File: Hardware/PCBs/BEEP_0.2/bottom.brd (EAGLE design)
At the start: 85.7 x 100 mm, 60 parts, among them IC1 74HCT00D, Q1 DMN2075U, Q2 IRLML2244, Q5 IRLML2244, Q6 IRLML2244, Q8 IRLML2244, U1 LM239AMDREP, U2 ATTINY10-TSHR

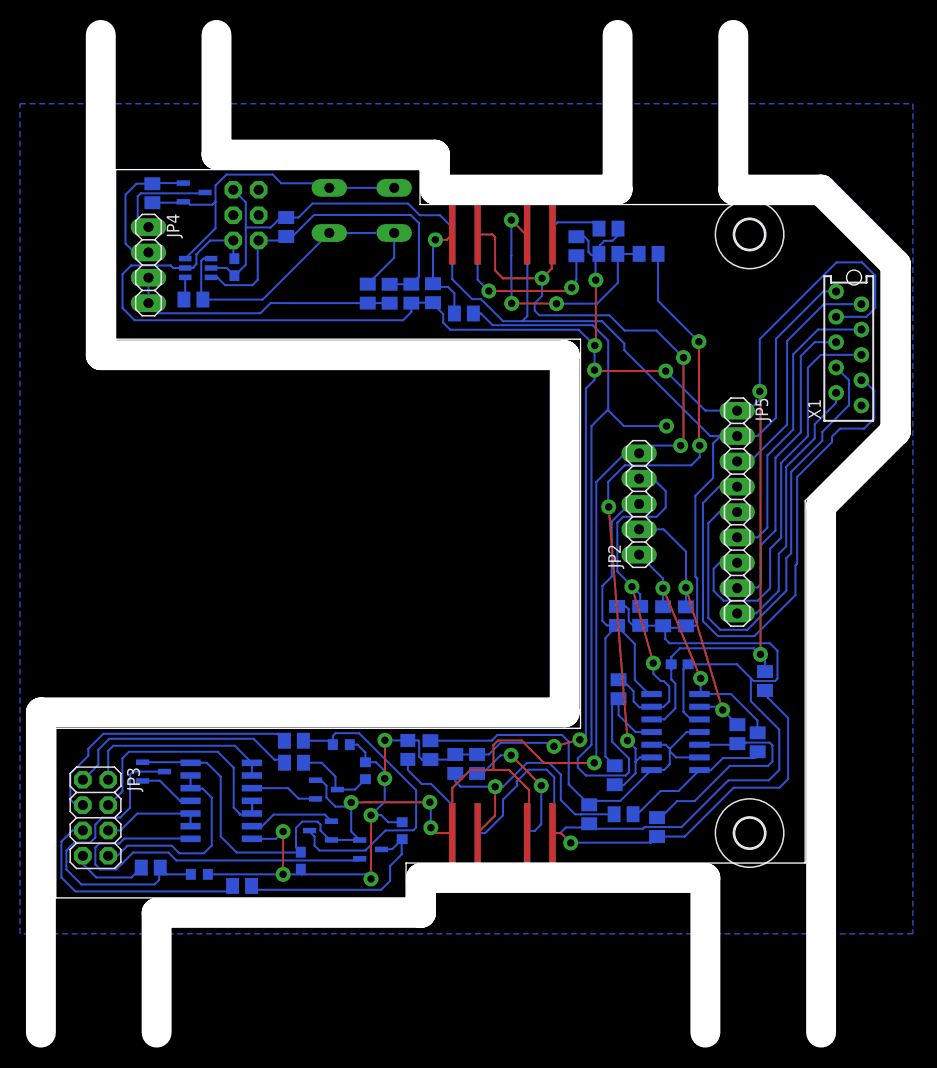
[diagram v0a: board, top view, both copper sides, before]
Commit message: correct encoder on bottom pcb enhance attiny code
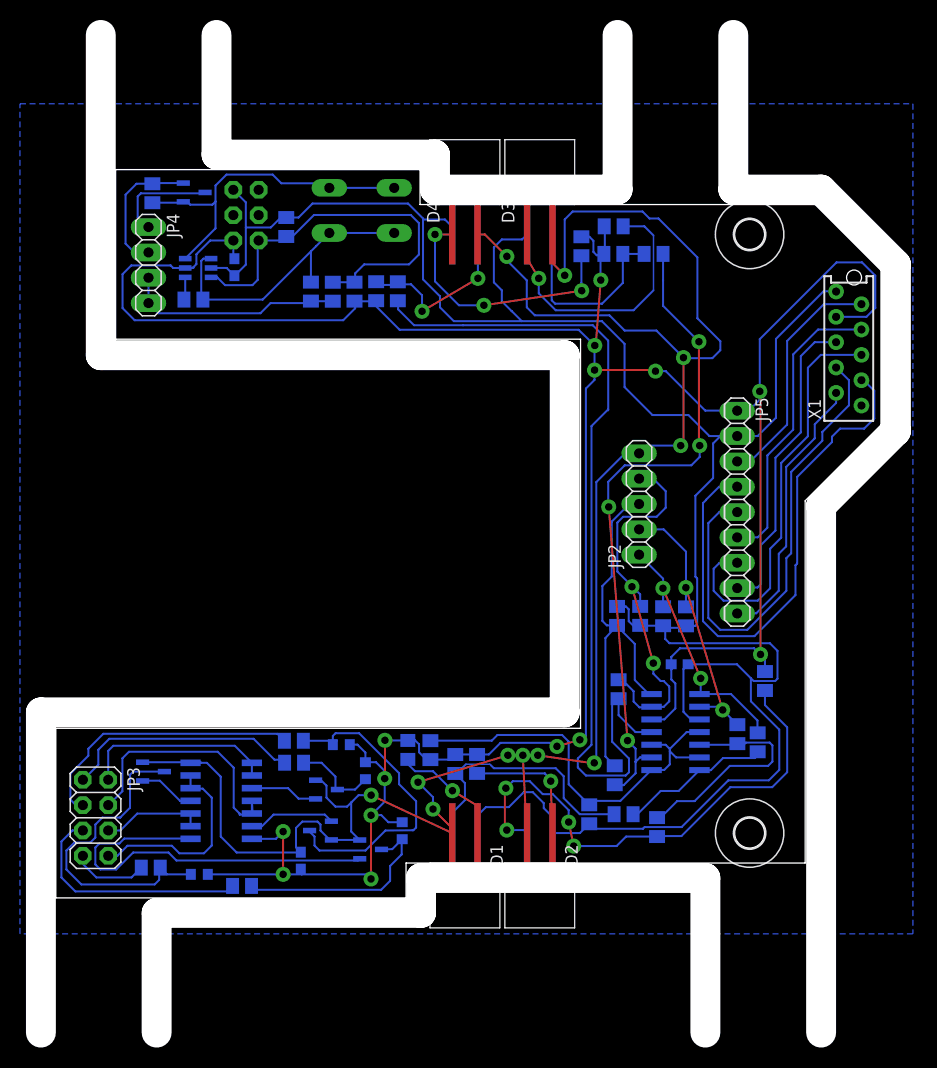
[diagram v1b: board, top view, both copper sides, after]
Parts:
- moved R29 6.99 mm to (37.3, 60.8), turned to 90 degrees
- moved R19 5.70 mm to (35.1, 60.8)
- moved R34 5.70 mm to (32.9, 60.8)
- moved R10 5.70 mm to (28.6, 60.8)
- moved R35 5.70 mm to (30.8, 60.8)
- moved R16 0.57 mm to (58.9, 67.3), turned to 180 degrees
- moved R17 0.50 mm to (58.9, 64.5)
- moved R18 0.50 mm to (55.7, 65.3)
- moved R28 0.50 mm to (62.9, 64.5)
- flipped D1 to the top
- flipped D2 to the top
- flipped D3 to the top
- flipped D4 to the top
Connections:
- net +3V3: now also D1.TRANS_C, D2.TRANS_C, D3.TRANS_C, D4.TRANS_C; no longer D1.LED_A, D2.LED_A, D3.LED_A, D4.LED_A
- net +5V: now also D1.LED_A, D2.LED_A, D3.LED_A, D4.LED_A; no longer D1.TRANS_C, D2.TRANS_C, D3.TRANS_C, D4.TRANS_C
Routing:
- net +5V: track 171.9 -> 203.4 mm, vias 7 -> 11
- net N$48: track 5.85 -> 28.7 mm, vias 0 -> 1
- net ENC_L2_RAW: track 36.5 -> 51.5 mm, vias 1 -> 4
- net ENC_R1_RAW: track 27.1 -> 19.8 mm, vias 3 -> 0
- net ENC_R2_RAW: track 11.1 -> 18.0 mm, vias 1 -> 2
- net +7V: track 27.6 -> 22.0 mm
- net +3V3: track 222.5 -> 227.8 mm
- net N$50: track 20.6 -> 25.7 mm, vias 2 -> 3
- net RESET: track 35.3 -> 40.1 mm
- net PB2/SOFT_OFF: track 34.2 -> 31.1 mm
- net N$43: track 9.81 -> 12.0 mm, vias 0 -> 1
- net N$49: track 85.3 -> 87.3 mm, vias 1 -> 0
- net N$46: track 14.1 -> 13.0 mm, vias 2 -> 1
- net GND: track 293.2 -> 292.2 mm
- net ENC_L1_RAW: track 26.9 -> 27.0 mm, vias 1 -> 0

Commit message: the forgotten commit ;)
* enhance bottom, rgb sensor pcb
* create attiny and lm239 eval boards
* bug fix for the pdf export scripts
* correct attiny soft power switch simulation
* add experimental color sensor code
* add rgb color look up table
* correct motor roations
* various other (this is the forgetten commit)
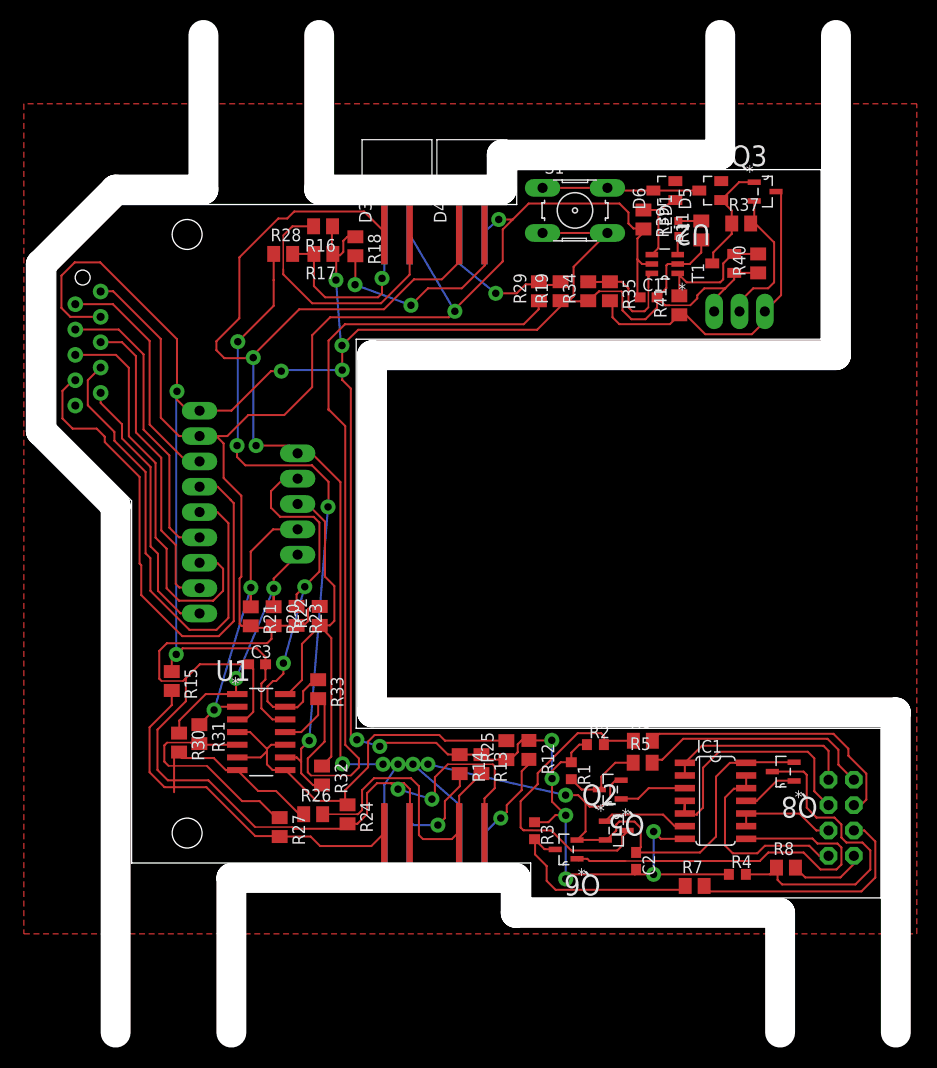
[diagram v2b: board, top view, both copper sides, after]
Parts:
- removed JP1: (no value), pinhead:2X03
- removed Q1: DMN2075U, BEEP:SOT95P240X112-3N
- removed R10: 100k, rcl:M0805
- removed R36: (no value), rcl:M0805
- removed R9: 1k, rcl:M0805
- added D5, D6: BAS40, diode:SOT23
- added LED1: (no value), led:CHIP-LED0603
- added Q3: IRLML2244, BEEP:SOT95P240X112-3N
- added R37, R41: 10k, rcl:M0805
- added R39: 100k, rcl:M0805
- added R40: 1k, rcl:M0805
- added T1: (no value), transistor:SOT23-EBC
- C2: value (none) -> 100n
- JP4: device pinhead:1X04 -> pinhead:1X03
- R11: value 1M -> 100R
- R12, R14, R16, R18: value (none) -> 330R
- R13, R15, R17, R19, R25: value (none) -> 10k
- R20, R21, R22, R23: value (none) -> 4.7k
- R24: value (none) -> 5.6k
- R26, R27, R28, R29: value (none) -> 100k
- R30, R31, R32, R33: value (none) -> 1M
- R5, R6, R7: value (none) -> 22R
- R8: value (none) -> 0
- moved X1 76.3 mm to (6.22, 55.1), flipped to the bottom
- moved JP3 74.7 mm to (81.7, 8.03), flipped to the bottom
- moved R8 63.7 mm to (76.2, 3.04), flipped to the top
- moved Q8 63.1 mm to (75.9, 12.7), flipped to the top
- moved R15 59.5 mm to (14.6, 21.7), flipped to the top
- moved JP4 59.4 mm to (71.5, 58.8), flipped to the bottom, turned to 0 degrees
- moved R30 58.0 mm to (15.3, 15.6), flipped to the top
- moved U$1 56.4 mm to (16.2, 6.50), flipped to the bottom
- moved U$2 56.4 mm to (16.2, 66.5), flipped to the bottom
- moved R11 55.1 mm to (67.7, 66.9), flipped to the top, turned to 90 degrees
- moved R4 53.9 mm to (71.3, 2.36), flipped to the top
- moved R31 53.9 mm to (17.4, 16.4), flipped to the top
- moved JP5 53.9 mm to (17.4, 38.7), flipped to the bottom
- moved IC1 49.5 mm to (69.1, 9.73), flipped to the top
- moved U2 46.8 mm to (64.0, 63.5), flipped to the top
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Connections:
- removed net +7V: JP4.3, JP4.4, R10.2, R35.2
- removed net BATT_GND: JP4.2, Q1.S, R11.1
- removed net PB0/TPIDATA: R9.1, U2.1
- removed net PB2/SOFT_OFF: R10.1, R9.2, S1.3, S1.4, U2.4
- removed net SWITCHED_GND: JP4.1, Q1.D
- removed net TPICLK: JP1.3
- removed net TPIDATA: JP1.1
- new net !OFF!: R40.2, R41.2, T1.B, U2.1
- new net BATT: JP4.2, Q3.S, R37.2
- new net N$6: LED1.C, R11.2
- new net N$8: D5.1, Q3.G, R37.1, T1.C
- new net N$9: D5.3, D6.3, S1.1, S1.2
- new net SENS: D6.1, R39.1, U2.4
- new net SWITCHED_BATT: JP4.1, Q3.D, R35.2, R41.1
- net +3V3: now also R39.2; no longer JP1.2, R36.2
- net GND: now also JP4.3, R11.1, R40.1, S1.3, S1.4, T1.E; no longer JP1.6
- net PB1/TPICLK: now also LED1.A; no longer Q1.G, R11.2, S1.1, S1.2
- net RESET: no longer JP1.5, R36.1
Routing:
- net SWITCHED_BATT: track 0.00 -> 33.2 mm
- net PB1/TPICLK: track 34.2 -> 1.90 mm
- net PB2/SOFT_OFF: track 31.1 -> 0.00 mm
- net RESET: track 40.1 -> 13.9 mm
- net +7V: track 22.0 -> 0.00 mm
- net N$9: track 0.00 -> 15.8 mm
- net ENC_L2_RAW: track 51.5 -> 36.2 mm, vias 4 -> 0
- net BATT: track 0.00 -> 14.7 mm
- net BATT_GND: track 13.8 -> 0.00 mm
- net !OFF!: track 0.00 -> 12.9 mm
- net N$8: track 0.00 -> 11.6 mm
- net +5V: track 203.4 -> 192.5 mm, vias 11 -> 8
- net SWITCHED_GND: track 10.6 -> 0.00 mm
- net GND: track 292.2 -> 300.9 mm
- net SENS: track 0.00 -> 8.21 mm
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- added copper zone on layer 1, net GND
- removed copper zone on layer 16, net GND
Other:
- outline, holes or cut-outs redrawn
